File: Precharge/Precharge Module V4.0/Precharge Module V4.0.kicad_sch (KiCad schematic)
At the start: 22 parts, among them J1 PH1-10-UA, Q1 SS8550, U1 NE555D, U2 IRLML2060TRPBF, U3 IRLML2060TRPBF, U4 IRLML2060TRPBF, U5 PMV160UP

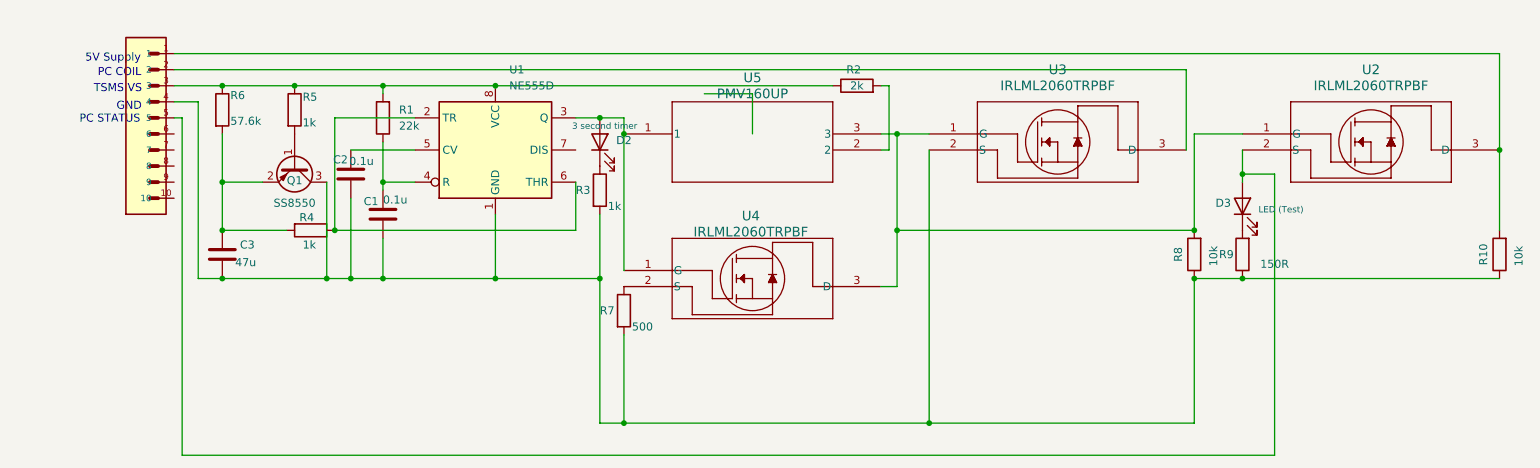
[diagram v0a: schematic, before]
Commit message: Precharge Changes
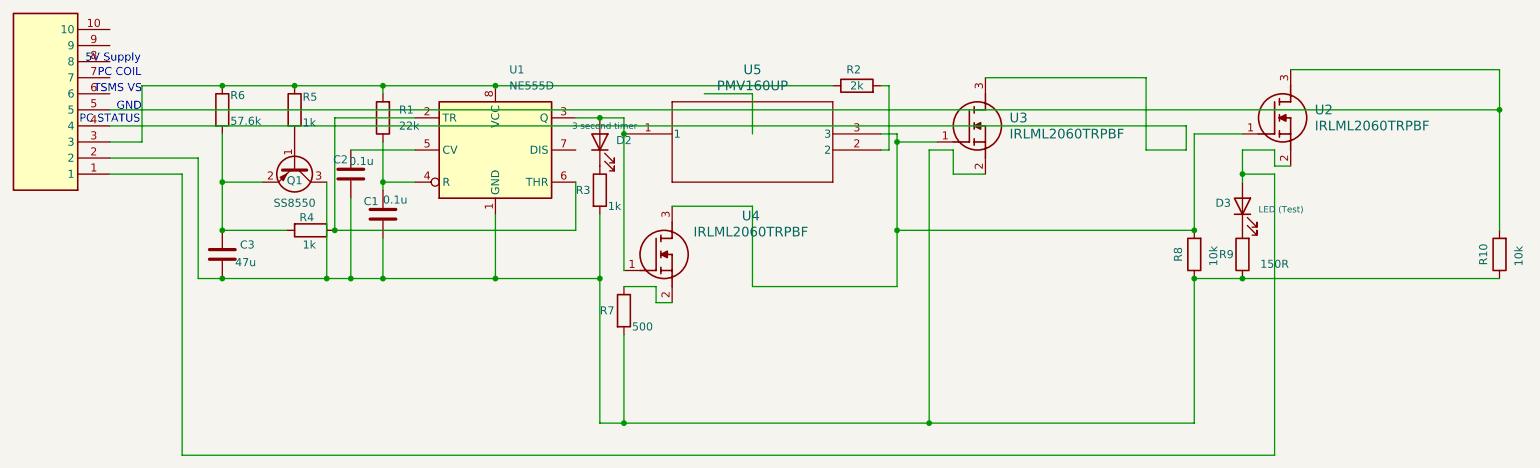
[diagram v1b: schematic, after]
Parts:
- J1: footprint 10 pin output:1X10-2.54MM-THT -> HDRV10W64P0X254_1X10_2540X249X886P; symbol 10 pin output:PH1-10-UA -> PH1-10-UA:PH1-10-UA; Arrow Part Number (none) -> PH1-10-UA; Arrow Price/Stock (none) -> null?utm_currency=USD&region=nac; Height (none) -> 8.865; Manufacturer_Name (none) -> Adam Tech; Manufacturer_Part_Number (none) -> PH1-10-UA; Mouser Part Number (none) -> 737-PH1-10-UA; Mouser Price/Stock (none) -> https://www.mouser.co.uk/ProductDetail/Adam-Tech/PH1-10-UA?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
- U2, U3, U4: footprint SOT23_INF -> SOT95P237X112-3N; symbol NMOS:IRLML2060TRPBF -> IRLML2060TRPBF:IRLML2060TRPBF; Arrow Part Number (none) -> IRLML2060TRPBF; Arrow Price/Stock (none) -> https://www.arrow.com/en/products/irlml2060trpbf/infineon-t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; Height (none) -> 1.12; Manufacturer_Name (none) -> Infineon; Manufacturer_Part_Number (none) -> IRLML2060TRPBF; Mouser Part Number (none) -> 942-IRLML2060TRPBF; Mouser Price/Stock (none) -> https://www.mouser.co.uk/ProductDetail/Infineon-Technologie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
- U5: symbol PMOS:PMV160UP -> 2025-09-16_20-26-56:PMV160UP
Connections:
- net at D3.2 (A), U2.2 (S): now also J1.1; no longer J1.5
- net at C1.2, C2.2, C3.2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: now also J1.2; no longer J1.4
- net at R10.2, U2.3 (D): now also J1.5; no longer J1.1
- net at U3.3 (D): now also J1.4; no longer J1.2

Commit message: Renaming stuff on boards that was wrong
RTDS schematic was totally totally wrong with the pins compared to the PCB
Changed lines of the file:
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@@
 (kicad_sch
-	(version 20231120)
+	(version 20250114)
 	(generator "eeschema")
-	(generator_version "8.0")
+	(generator_version "9.0")
 	(paper "A4")
+	(text "GND"
+		(exclude_from_sim no)
+		(at 33.02 36.322 0)
+		(effects
+			(font
+				(size 1.27 1.27)
+			)
+		)
+	)
+	(text "PC COIL"
+		(exclude_from_sim no)
+		(at 31.496 30.988 0)
+		(effects
+			(font
+				(size 1.27 1.27)
+			)
+		)
+	)
+	(text "TSMS VS"
+		(exclude_from_sim no)
+		(at 31.242 33.528 0)
+		(effects
+			(font
+				(size 1.27 1.27)
+			)
+		)
+	)
+	(text "PC STATUS"
+		(exclude_from_sim no)
+		(at 29.972 38.354 0)
+		(effects
+			(font
+				(size 1.27 1.27)
+			)
+		)
+	)
+	(text "5V Supply"
+		(exclude_from_sim no)
+		(at 30.48 28.702 0)
+		(effects
+			(font
+				(size 1.27 1.27)
+			)
+		)
+	)
 	(junction
 		(at 109.22 30.48)
@@
 			(width 0)
 			(type default)
-		)
-	)
-	(text "GND"
-		(exclude_from_sim no)
-		(at 34.798 28.702 0)
-		(effects
-			(font
-				(size 1.27 1.27)
-			)
-		)
-	)
-	(text "PC COIL"
-		(exclude_from_sim no)
-		(at 33.274 23.368 0)
-		(effects
-			(font
-				(size 1.27 1.27)
-			)
-		)
-	)
-	(text "TSMS VS"
-		(exclude_from_sim no)
-		(at 33.02 25.908 0)
-		(effects
-			(font
-				(size 1.27 1.27)
-			)
-		)
-	)
-	(text "PC STATUS"
-		(exclude_from_sim no)
-		(at 31.75 30.734 0)
-		(effects
-			(font
-				(size 1.27 1.27)
-			)
-		)
-	)
-	(text "5V Supply"
-		(exclude_from_sim no)
-		(at 32.258 21.082 0)
-		(effects
-			(font
-				(size 1.27 1.27)
-			)
 		)
 	)
@@
 		)
 	)
+	(embedded_fonts no)
 )
